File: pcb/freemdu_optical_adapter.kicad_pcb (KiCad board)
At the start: 2 copper layers, 55.1 x 36.1 mm, 20 parts, among them J1 Conn_01x04, J2 Conn_01x04, J3 Conn_01x07, J4 Conn_01x07, J5 Conn_01x02, J6 Conn_01x04, Q1 BSS138, Q2 BSS138, U1 SFH7250, U3 74LVC1G17GW,125

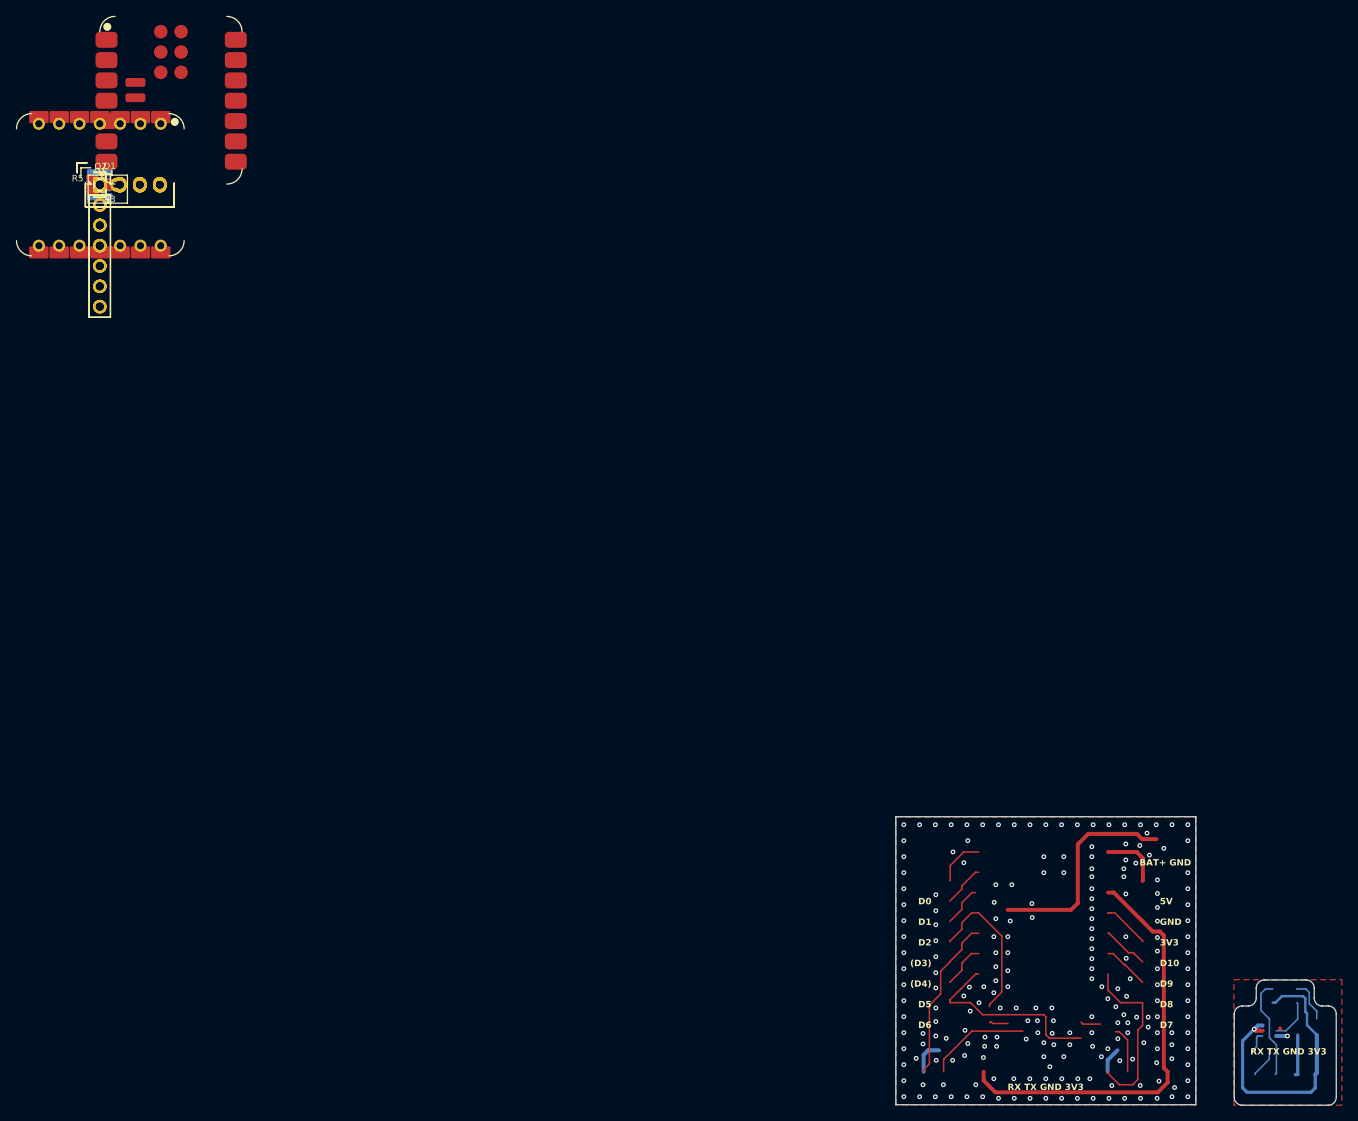
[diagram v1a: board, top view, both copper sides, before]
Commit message: fix missing pulldowns for nmos-gates
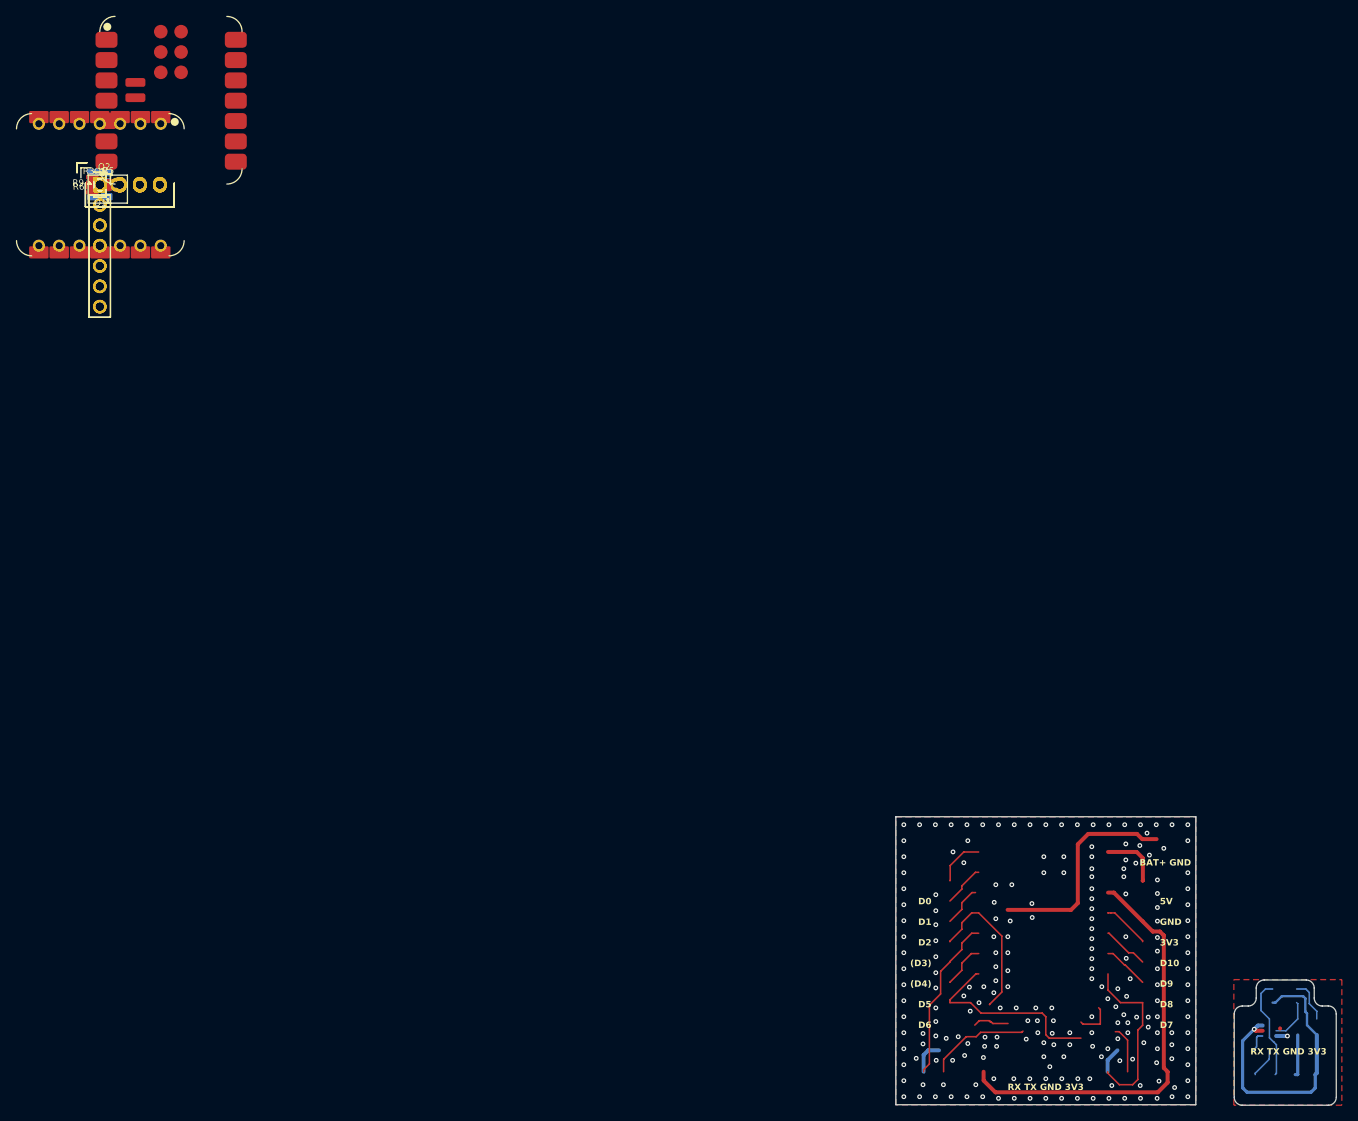
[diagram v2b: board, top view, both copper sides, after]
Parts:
- added R6, R9: 47k, Resistor_SMD:R_0805_2012Metric_Pad1.20x1.40mm_HandSolder, F.Cu at (0.00, 0.00)
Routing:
- net Net-(Q2-G): track 2.52 -> 4.66 mm
- net Net-(Q1-G): track 2.43 -> 4.55 mm
